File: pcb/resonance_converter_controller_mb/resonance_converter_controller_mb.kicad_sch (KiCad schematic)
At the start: 36 parts, among them J3 Conn_01x02, Q1 Q_NPN_BEC, Q2 Q_NPN_BEC, Q3 Q_PMOS_GDS, U1 PCF8574RGTR, U2 TL431D, U3 74LVC1G04

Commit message: _mb board freerouted
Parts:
- added D7, D8: D, Diode_SMD:D_SMA, symbol Device:D
- added J5, J6: Conn_01x04_MountingPin, Connector_JST:JST_SH_SM04B-SRSS-TB_1x04-1MP_P1.00mm_Horizontal, symbol Connector_Generic_MountingPin:Conn_01x04_MountingPin
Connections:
- net EXT_VCC: now also D7.1 (K), D8.1 (K)
- net GND: now also J5.1 (Pin_1), J5.MP (MountPin), J6.1 (Pin_1), J6.MP (MountPin)
- net I2C_EXT_SCL: now also J5.4 (Pin_4)
- net I2C_EXT_SDA: now also J5.3 (Pin_3)
- new net: D8.2 (A), J6.2 (Pin_2)
- new net: D7.2 (A), J5.2 (Pin_2)
- new net DOCK_CTRL_RX: J6.4 (Pin_4)
- new net DOCK_CTRL_TX: J6.3 (Pin_3)

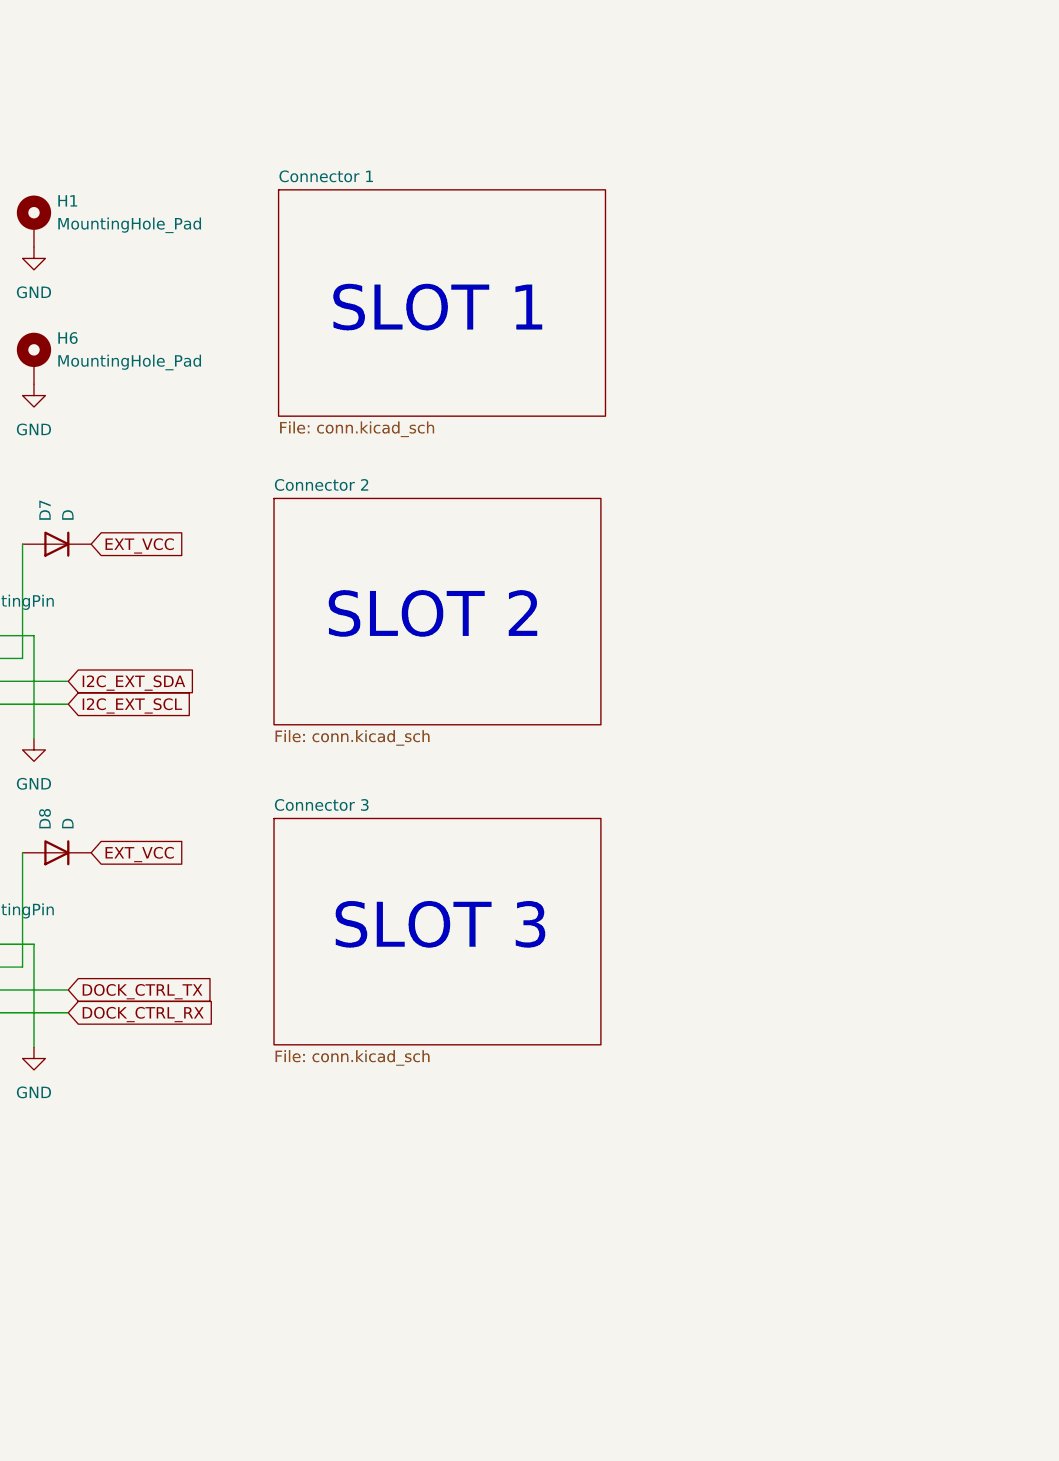
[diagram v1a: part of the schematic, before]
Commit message: Add I2C line terminator
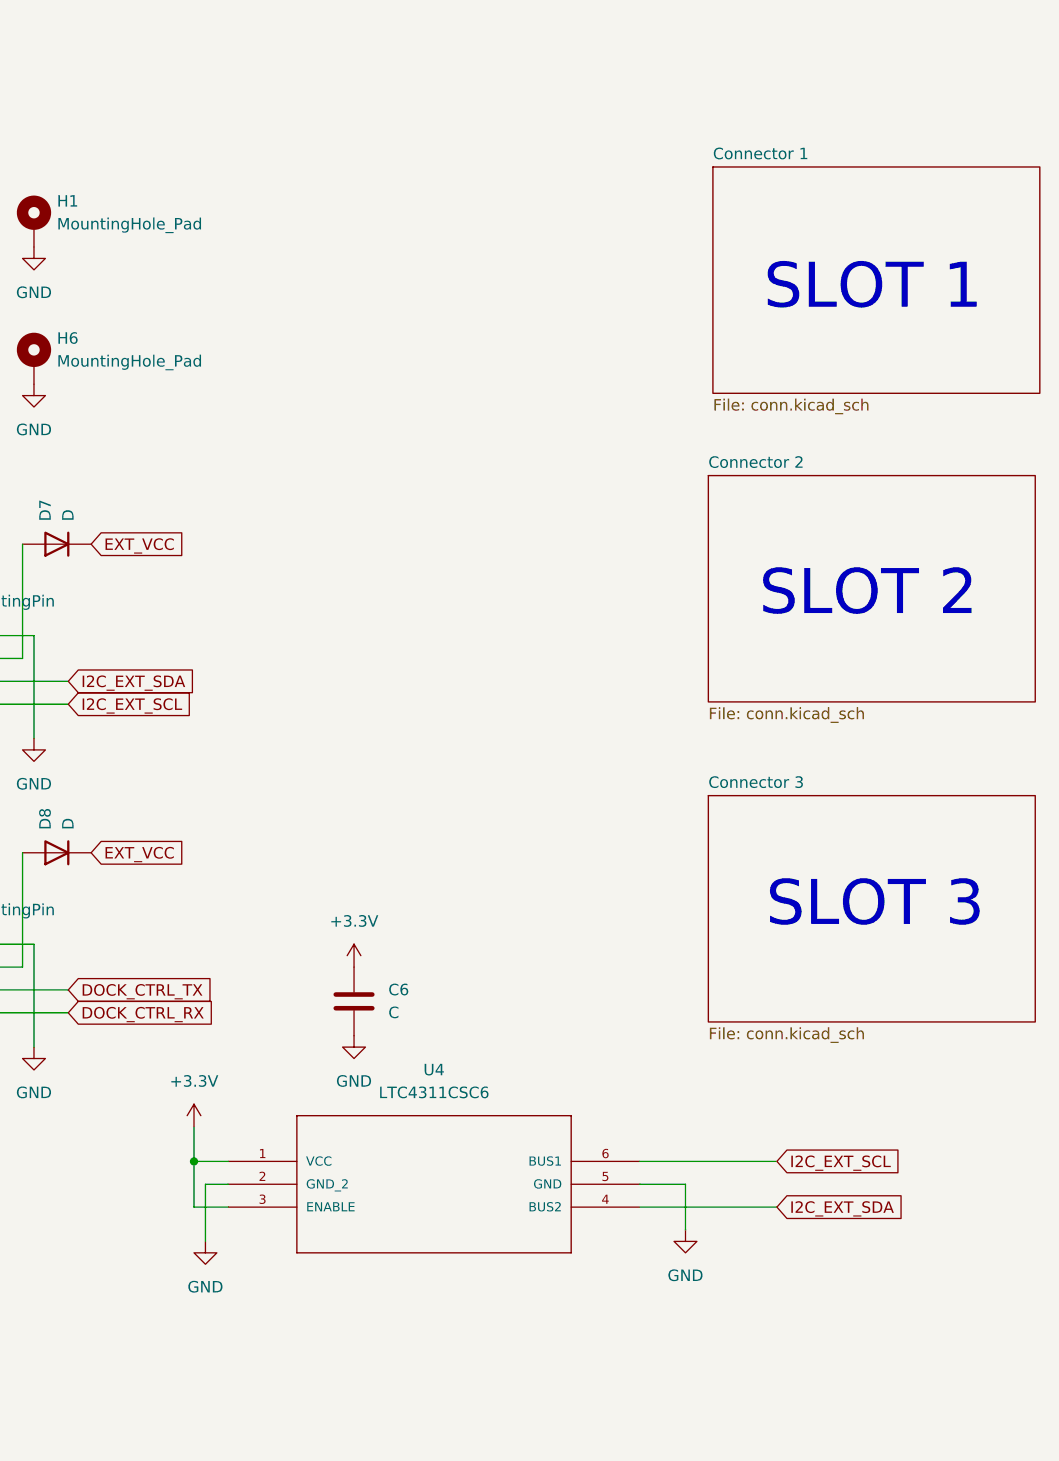
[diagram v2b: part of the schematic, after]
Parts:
- added C6: C, Capacitor_SMD:C_0805_2012Metric, symbol Device:C
- added U4: LTC4311CSC6, LTC4311CSC6:SC70-SC6, symbol LTC4311CSC6:LTC4311CSC6
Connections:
- net +3.3V: now also C6.1, U4.1 (VCC), U4.3 (ENABLE)
- net GND: now also C6.2, U4.2 (GND_2), U4.5 (GND)
- net I2C_EXT_SCL: now also U4.6 (BUS1)
- net I2C_EXT_SDA: now also U4.4 (BUS2)

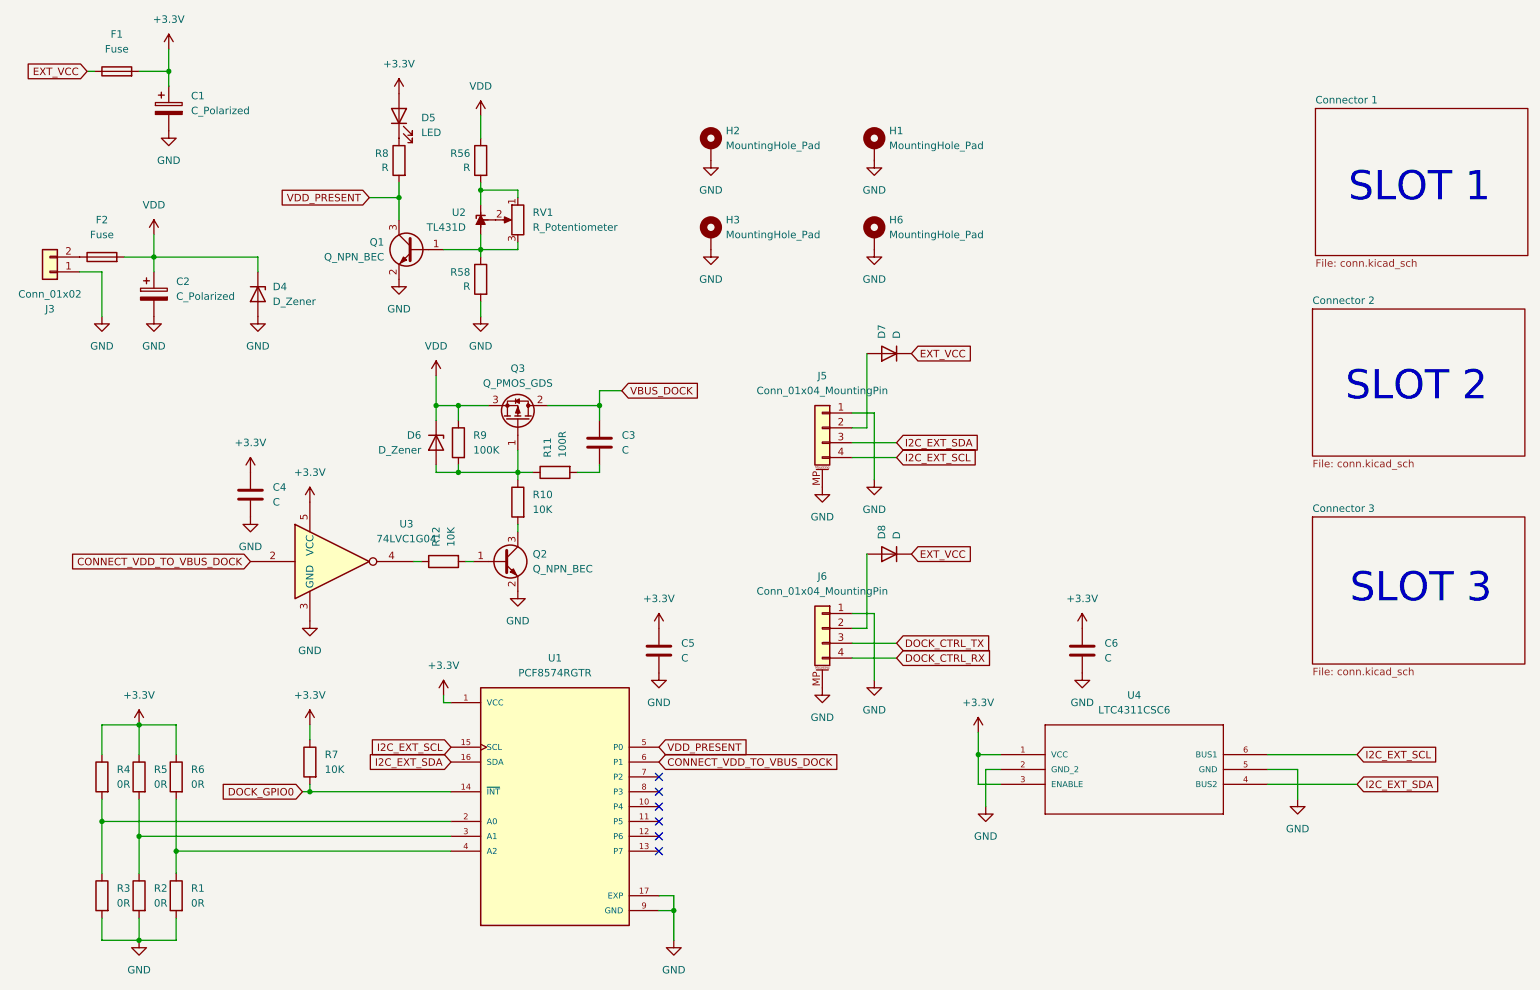
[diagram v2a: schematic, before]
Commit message: Add 3.3v regulator and fix silkscreen
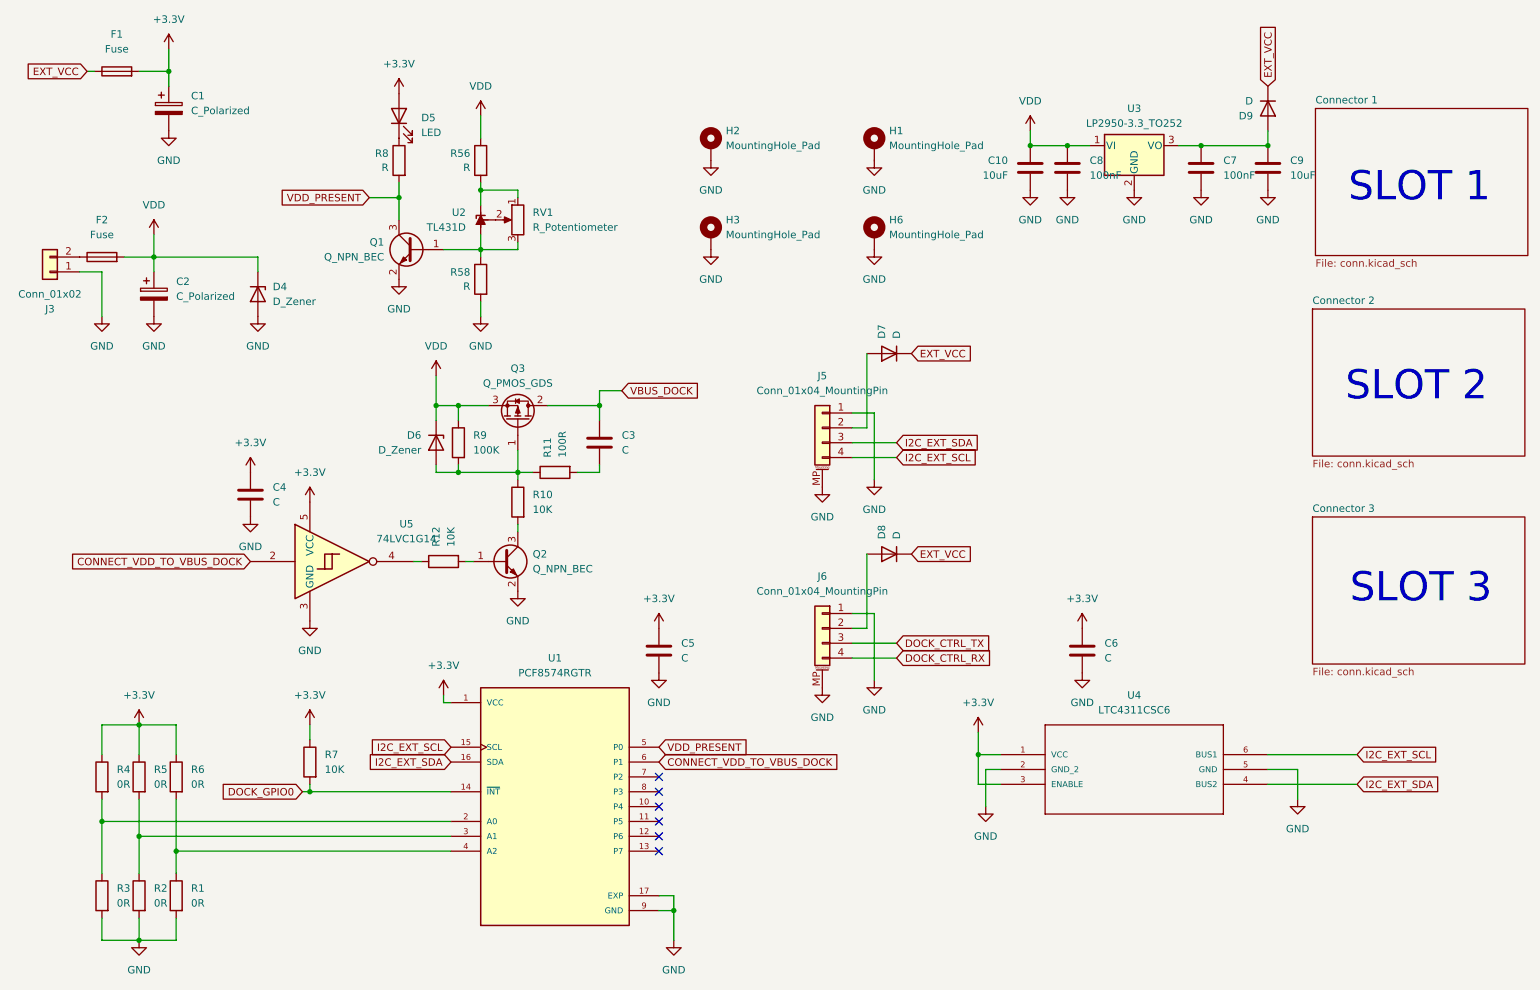
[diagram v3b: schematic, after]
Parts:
- removed U3: 74LVC1G04, Package_TO_SOT_SMD:SOT-23-5, symbol 74xGxx:74LVC1G04
- added C10, C9: 10uF, Capacitor_SMD:C_0805_2012Metric, symbol Device:C
- added C7, C8: 100nF, Capacitor_SMD:C_0805_2012Metric, symbol Device:C
- added D9: D, Diode_SMD:D_SMA, symbol Device:D
- added U3: LP2950-3.3_TO252, Package_TO_SOT_SMD:TO-252-2, symbol Regulator_Linear:LP2950-3.3_TO252
- added U5: 74LVC1G14, symbol 74xGxx:74LVC1G14
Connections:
- net +3.3V: now also U5.5 (VCC)
- net CONNECT_VDD_TO_VBUS_DOCK: now also U5.2
- net EXT_VCC: now also D9.1 (K)
- net GND: now also C10.2, C7.2, C8.2, C9.2, U3.2 (GND), U5.3 (GND)
- net VDD: now also C10.1, C8.1, U3.1 (VI)
- net at R12.1: now also U5.4
- new net: C7.1, C9.1, D9.2 (A), U3.3 (VO)
